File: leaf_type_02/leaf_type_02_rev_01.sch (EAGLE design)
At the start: 25 parts, among them J1 TC_2050_IDC_NL_TOP, J3 CONN_4X1_JST_PA, J4 CONN_4X1_JST_PA, J5 CONN_4X1_LEAF_SMT, U2 RS485_XCVR_SN65HVD178X

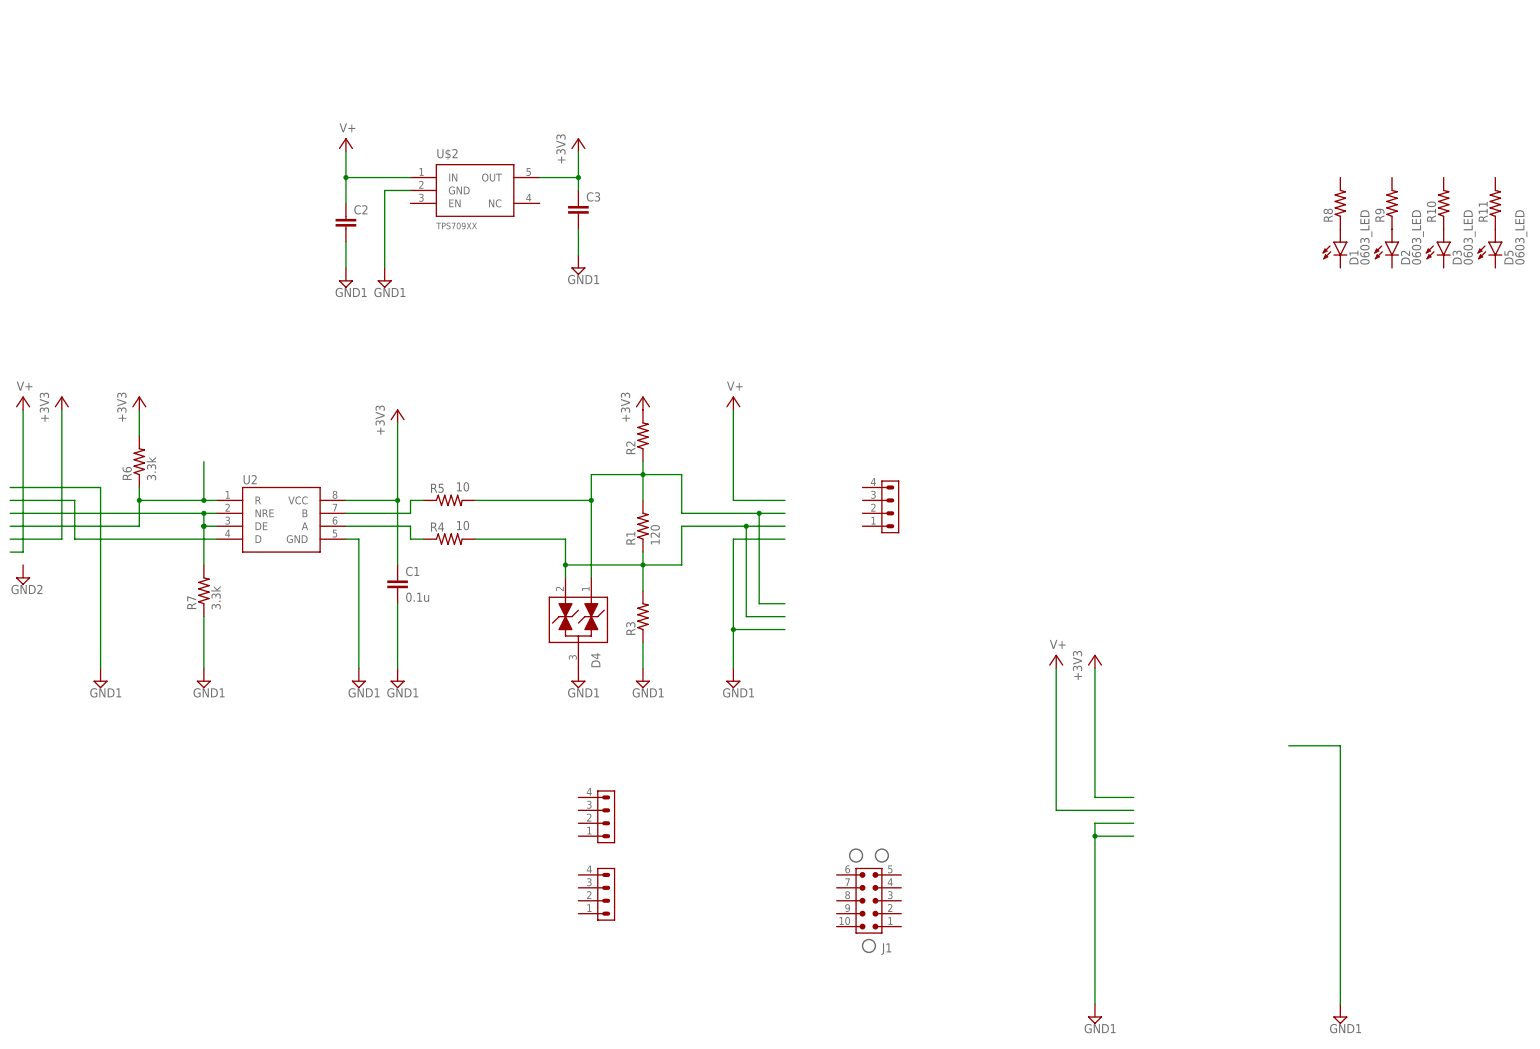
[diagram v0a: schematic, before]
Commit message: updated library & type 02
fixed some of the sizes of device names, updates rs485 tx & rx drivers
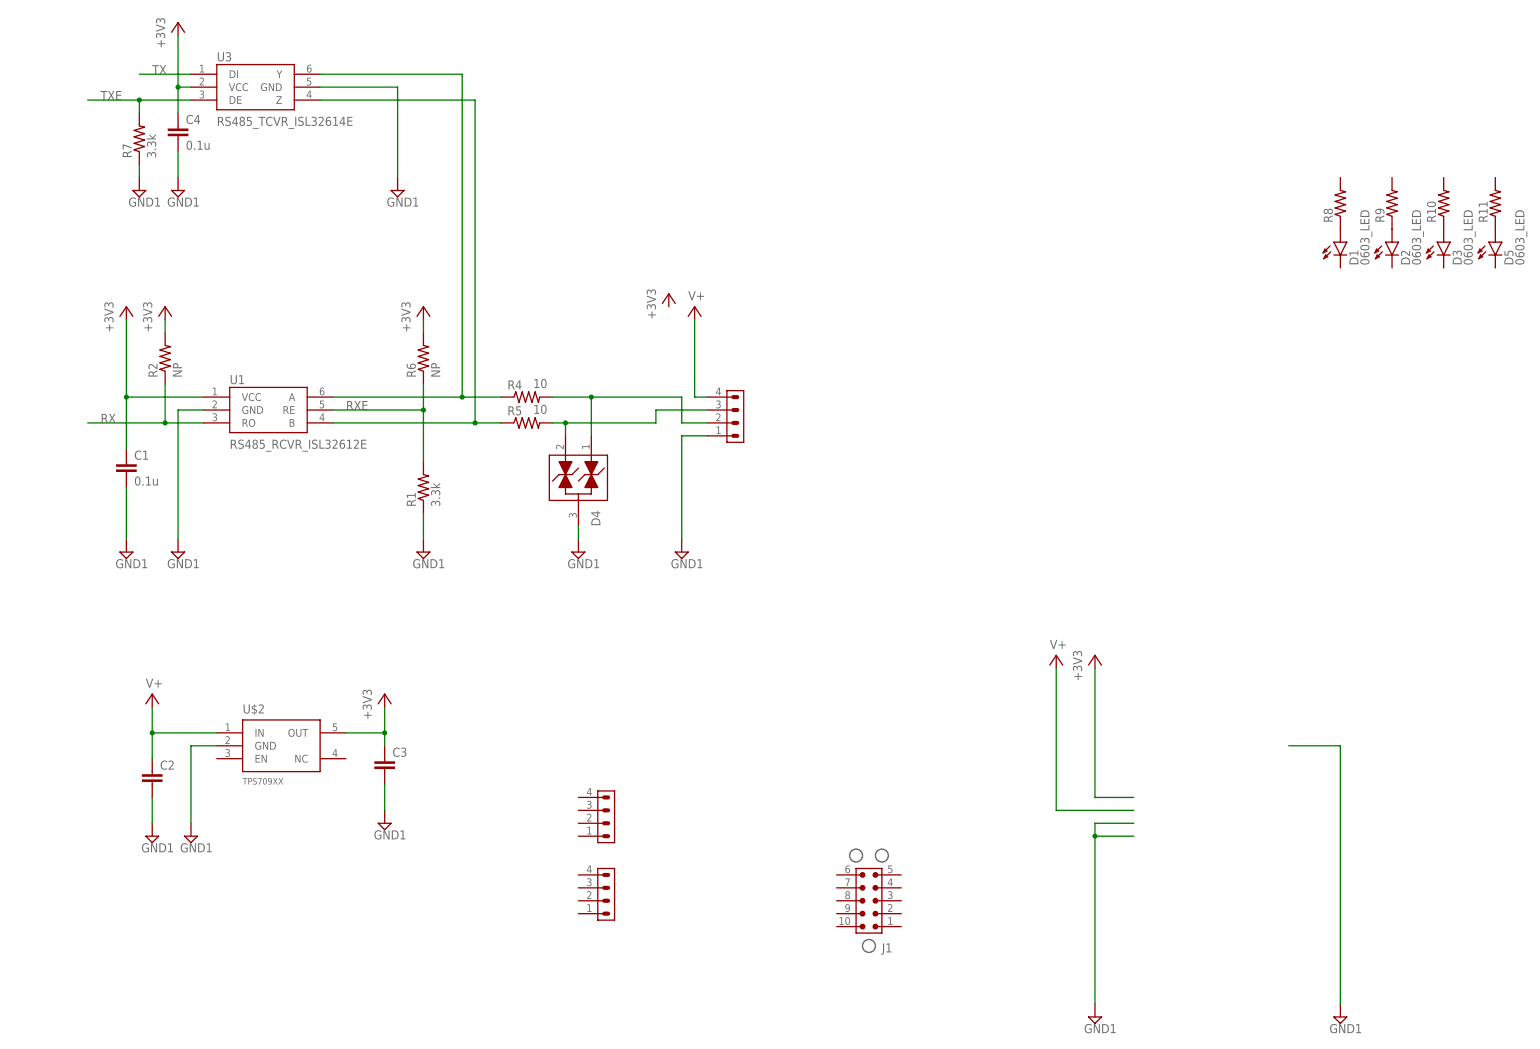
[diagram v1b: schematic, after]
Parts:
- removed R3: (no value), stepOSP:0603_RES
- removed U2: RS485_XCVR_SN65HVD178X, leaf:RS485_XCVR_SN65HVD178X
- added C4: 0.1u, stepOSP:0603_CAP
- added U1: RS485_RCVR_ISL32612E, leaf:RS485_RCVR_ISL32612E
- added U3: RS485_TCVR_ISL32614E, leaf:RS485_TCVR_ISL32614E
- R1: value 120 -> 3.3k
- R2: value (none) -> NP
- R6: value 3.3k -> NP
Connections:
- removed net N$10: U2.D
- removed net N$6: D4.2, R1.1, R3.2, R4.2
- removed net N$9: R6.1, U2.R
- new net RX: R2.1, U1.RO
- new net RXE: R1.2, R6.1, U1.RE
- new net TX: U3.DI
- new net TXE: R7.2, U3.DE
- net +3V3: now also C4.1, U1.VCC, U3.VCC; no longer U2.VCC
- net GND1: now also C4.2, J5.1, R1.1, U1.GND, U3.GND; no longer R3.1, U2.GND
- net N$1: now also U1.A, U3.Y; no longer U2.A
- net N$2: now also U1.B, U3.Z; no longer U2.B
- net N$7: now also D4.2, J5.3; no longer D4.1, R1.2, R2.1
- net N$8: now also D4.1, J5.2, R4.2; no longer R7.2, U2.DE, U2.NRE
- net V+: now also J5.4
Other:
- moved on the sheet: C1, C2, C3, D4, R1, R2, R4, R5, R6, R7, U$2

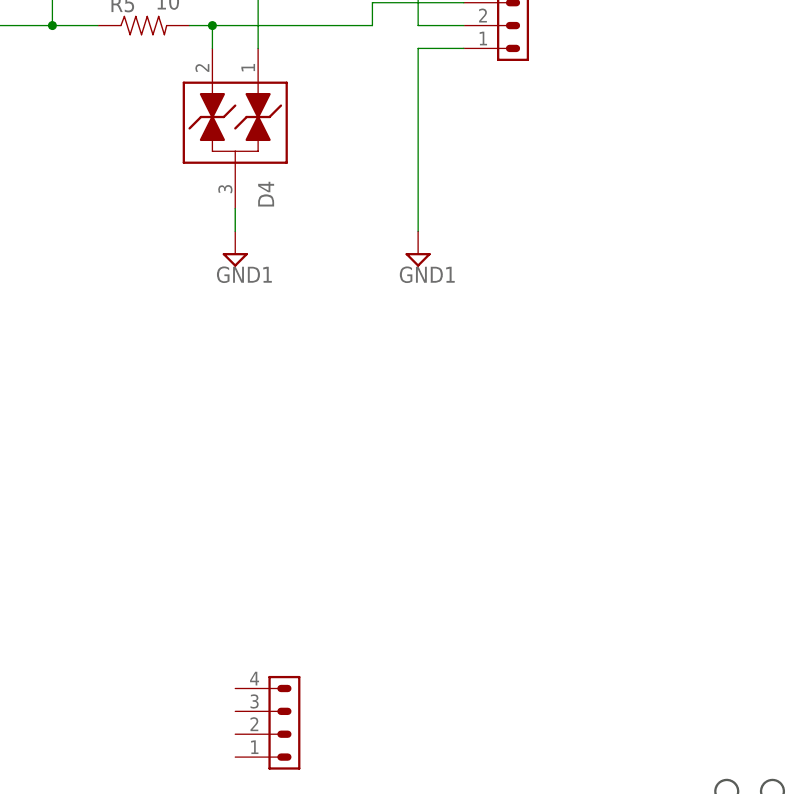
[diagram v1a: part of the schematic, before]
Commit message: added to library GH connector and updated 0x02 board layout
gh connector only can handle 1A which isn't great but very small
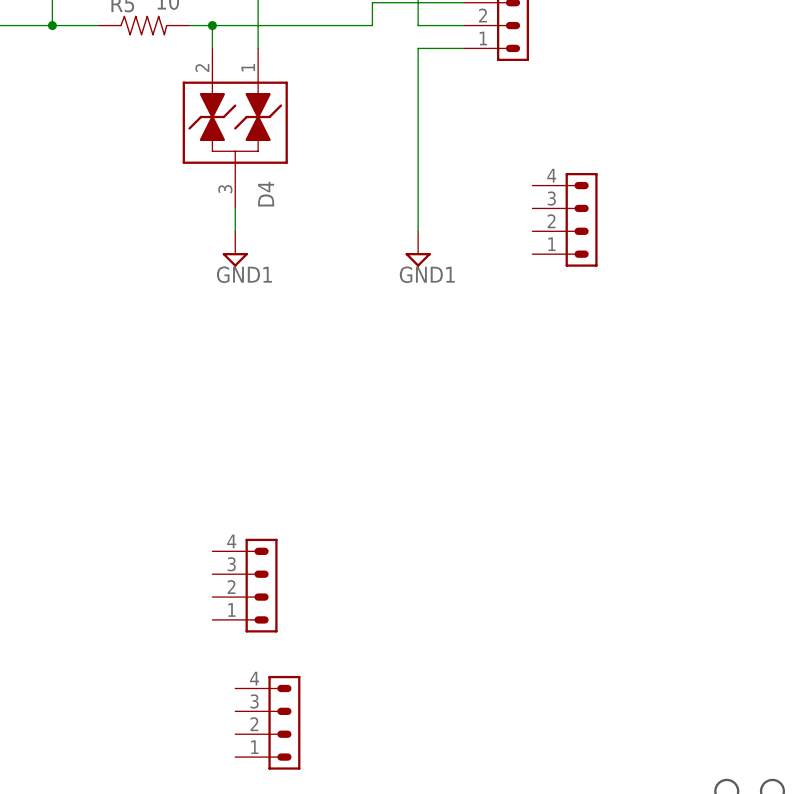
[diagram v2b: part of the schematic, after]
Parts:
- added J2: CONN_4X1_LEAF_SMT, leaf:CONN_4X1_LEAF_SMT
- added J6: CONN_4X1_JST_GH, leaf:CONN_4X1_JST_GH
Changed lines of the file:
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@@
 <part name="+3V1" library="supply1" deviceset="+3V3" device=""/>
 <part name="SUPPLY3" library="supply2" deviceset="GND1" device=""/>
+<part name="J2" library="leaf" deviceset="CONN_4X1_LEAF_SMT" device=""/>
+<part name="J6" library="leaf" deviceset="CONN_4X1_JST_GH" device=""/>
 </parts>
 <sheets>
@@
 <instance part="+3V1" gate="G$1" x="91.44" y="175.26"/>
 <instance part="SUPPLY3" gate="G$1" x="193.04" y="127"/>
+<instance part="J2" gate="G$1" x="210.82" y="127"/>
+<instance part="J6" gate="G$1" x="175.26" y="86.36"/>
 </instances>
 <busses>

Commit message: WORK IN PROGRESS
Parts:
- removed C1: 0.1u, stepOSP:0603_CAP
- removed J1: TC_2050_IDC_NL_TOP, leaf:TC_2050_IDC_NL_TOP
- removed J4: CONN_4X1_JST_PA, leaf:CONN_4X1_JST_PA
- removed J5: CONN_4X1_LEAF_SMT, leaf:CONN_4X1_LEAF_SMT
- removed R2, R6: NP, stepOSP:0603_RES
- removed U3: RS485_TCVR_ISL32614E, leaf:RS485_TCVR_ISL32614E
- J2: value CONN_4X1_LEAF_SMT -> TC_2030_IDC_NL_TOP; device leaf:CONN_4X1_LEAF_SMT -> leaf:TC_2030_IDC_NL_TOP
- J3: value CONN_4X1_JST_PA -> CONN_4X1_JST_GH; device leaf:CONN_4X1_JST_PA -> leaf:CONN_4X1_JST_GH
- U1: value RS485_RCVR_ISL32612E -> RS485_XCVR_SN65HVD178X; device leaf:RS485_RCVR_ISL32612E -> leaf:RS485_XCVR_SN65HVD178X
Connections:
- removed net N$11: D5.A, R11.1
- removed net N$8: D4.1, J5.2, R4.2
- removed net RX: R2.1, U1.RO
- removed net RXE: R1.2, R6.1, U1.RE
- removed net TX: U3.DI
- removed net TXE: R7.2, U3.DE
- new net N$10: R7.2, U1.DE, U1.NRE
- new net N$12: R1.1, U1.R
- new net N$13: U1.D
- new net N$6: R4.1, U1.B
- new net N$9: R5.1, U1.A
- net +3V3: now also D1.A, D2.A, D3.A, D5.A, R1.2; no longer C1.1, R2.2, R6.2, U3.VCC
- net GND1: now also J3.1, J6.1; no longer C1.2, J5.1, R1.1, U3.GND
- net N$1: now also D4.1, J3.3, J6.3, R4.2; no longer R4.1, U1.A, U3.Y
- net N$2: now also D1.C, R8.2; no longer R5.1, U1.B, U3.Z
- net N$3: now also D2.C, R9.2; no longer D1.A, R8.1
- net N$4: now also D3.C, R10.2; no longer D2.A, R9.1
- net N$5: now also D5.C, R11.2; no longer D3.A, R10.1
- net N$7: now also J3.2, J6.2; no longer J5.3
- net V+: now also J3.4; no longer J5.4
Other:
- moved on the sheet: C4, D1, D2, D3, D5, R1, R10, R11, R7, R8, R9

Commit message: updating 0x02 build
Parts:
- removed D3, D5: 0603_LED, stepOSP:0603_LED
- removed J3, J6: CONN_4X1_JST_GH, leaf:CONN_4X1_JST_GH
- removed R10, R11: (no value), stepOSP:0603_RES
- added J1: TC_2050_IDC_NL_TOP, leaf:TC_2050_IDC_NL_TOP
- added J4, J5: CONN_4X1_JST_PA, leaf:CONN_4X1_JST_PA
- J2: value TC_2030_IDC_NL_TOP -> CONN_5X2_0P05_IN_SMT; device leaf:TC_2030_IDC_NL_TOP -> leaf:CONN_5X2_0P05_IN_SMT
- R1, R7, R8, R9: device stepOSP:0603_RES -> stepOSP:0402_RES
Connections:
- removed net N$4: D3.C, R10.2
- removed net N$5: D5.C, R11.2
- net +3V3: no longer D3.A, D5.A
- net GND1: now also J4.2, J5.3; no longer J3.1, J6.1
- net N$1: now also J4.4, J5.1; no longer J3.3, J6.3
- net N$7: now also J4.3, J5.2; no longer J3.2, J6.2
- net V+: now also J4.1, J5.4; no longer J3.4
